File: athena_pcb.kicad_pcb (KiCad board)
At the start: 2 copper layers, 40.5 x 23.8 mm, 36 parts, among them J2 Conn_01x04, SW1 SW_Push, U1 NRF5340-QKAA-R7, U2 BME280, Y1 32MHz, Y2 32.768kHz

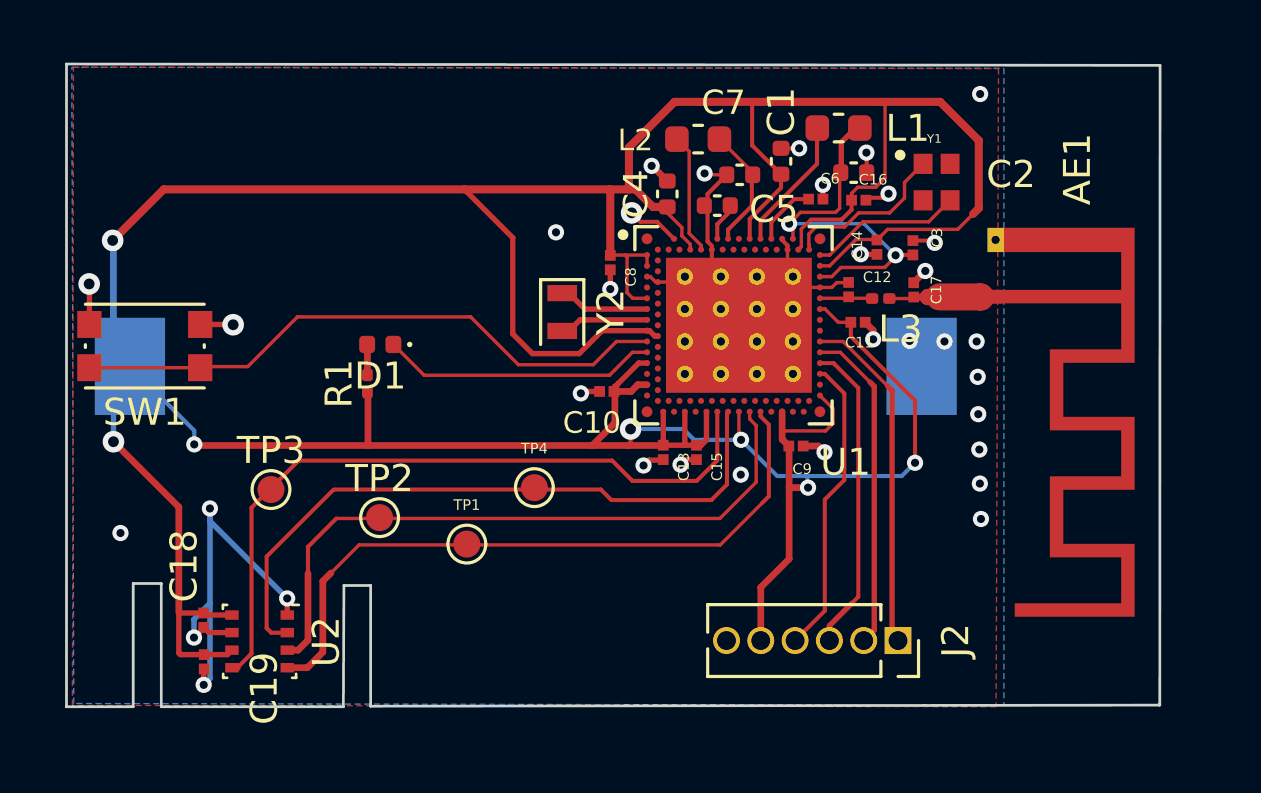
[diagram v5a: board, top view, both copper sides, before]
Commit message: Updated tracks to 6mils where possible
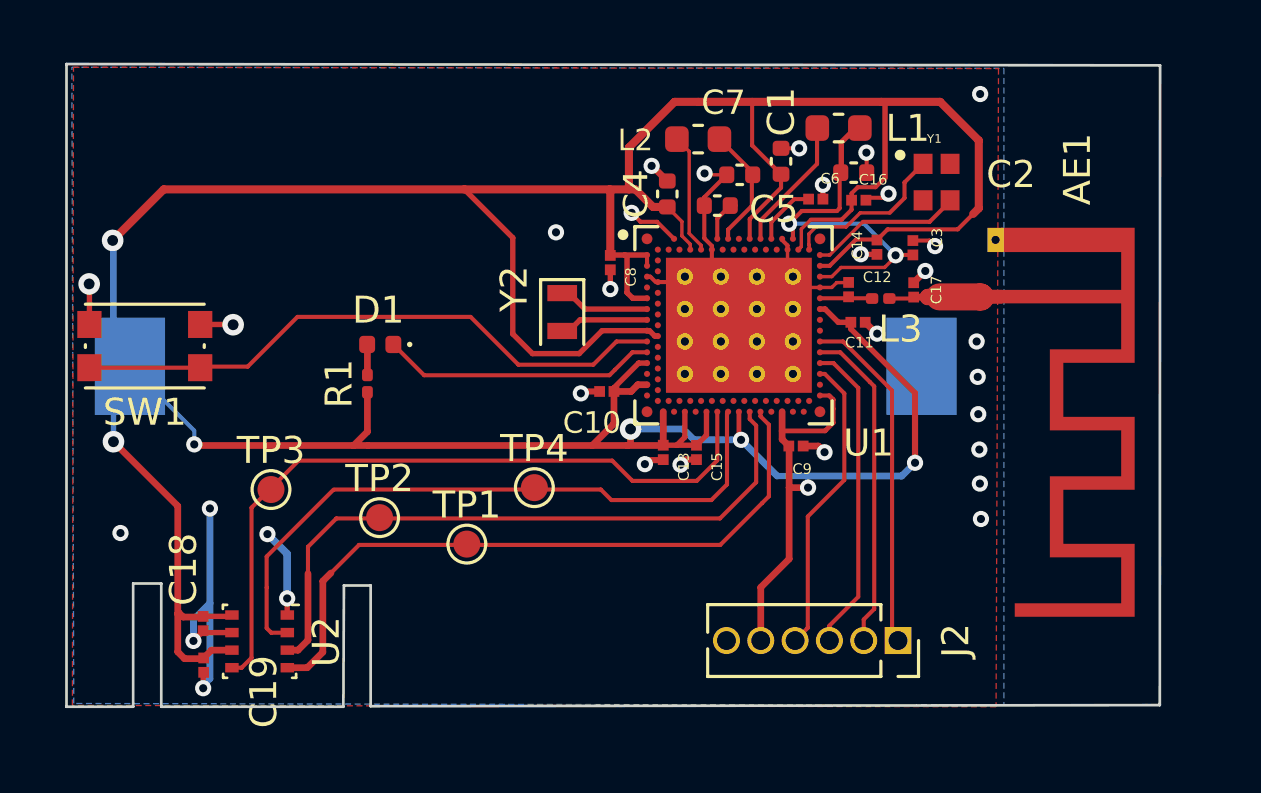
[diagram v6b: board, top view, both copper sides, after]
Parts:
- moved C19 0.13 mm to (96.5, 103.3)
- moved C18 0.13 mm to (96.5, 101.8)
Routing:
- net GND: track 51.3 -> 49.7 mm, vias 34 -> 32

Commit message: Added edge clearence, transmission line width to match with pcb antenna feed
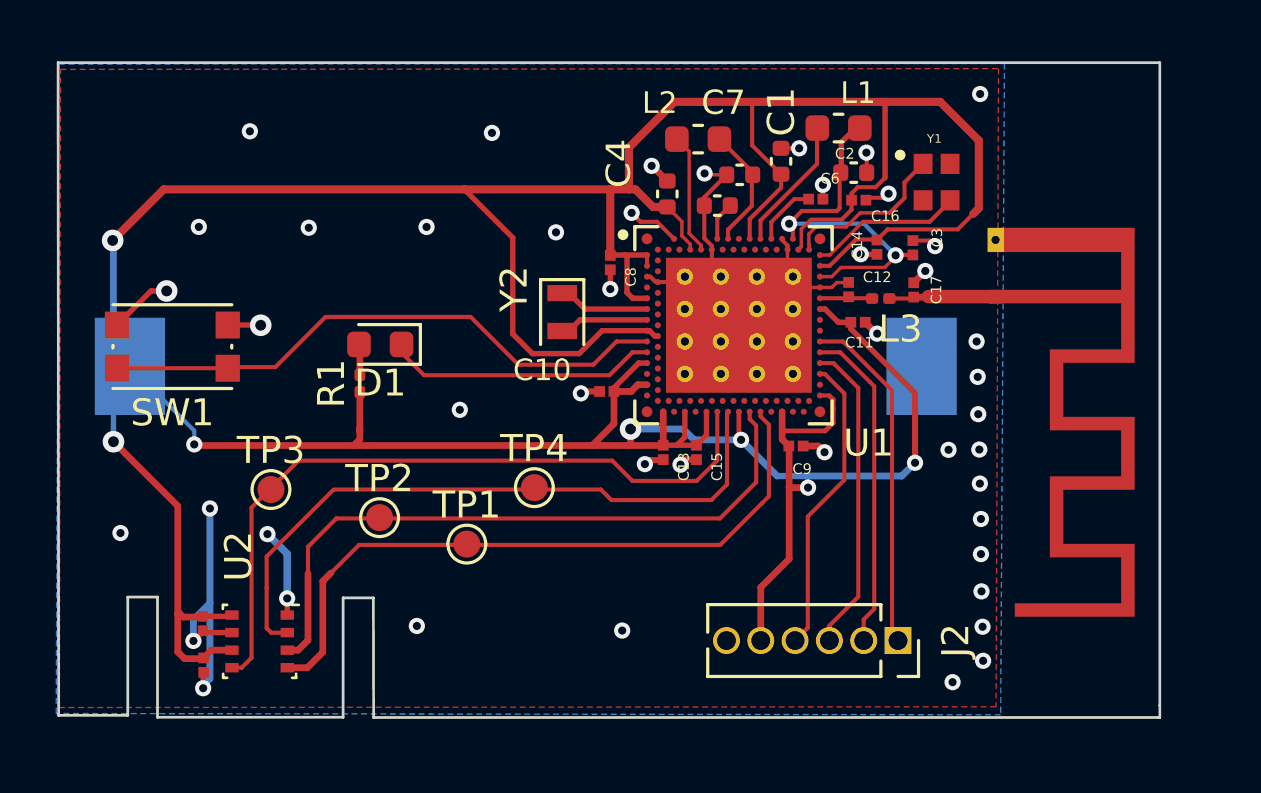
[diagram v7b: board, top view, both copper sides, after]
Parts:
- C5, C7: value 1.0uF -> 1uF
- D1: footprint LED_SMD:LED_0402_1005Metric -> LED_SMD:LED_0603_1608Metric
- moved SW1 1.02 mm to (95.4, 91.5)
- moved R1 0.28 mm to (102.3, 92.9)
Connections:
- U1 pad AK20: /P0.23 -> unconnected-(U1C-P0.23-PadAK20)
- U1 pad AL27: /P0.24 -> unconnected-(U1C-P0.24-PadAL27)
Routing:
- net GND: track 49.7 -> 51.0 mm, vias 32 -> 46
- net /P0.02: track 22.5 -> 21.5 mm
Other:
- board size 40.5 x 23.8 mm -> 40.8 x 24.2 mm

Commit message: Version sent to PCB manufacturer
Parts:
- added REF**: MountingHole_2.2mm_M2_DIN965, MountingHole:MountingHole_2.2mm_M2_DIN965, F.Cu at (94.6, 84.0)
- L1, L2: footprint Inductor_SMD:L_0603_1608Metric -> LQM18DN100M70L:INDC1608X95N
- L3: footprint Inductor_SMD:L_0201_0603Metric -> LQP03HQ2N2B02D:IND_LQP03HQ2N2B02D
- R1: value 220R -> 200R; footprint Resistor_SMD:R_0201_0603Metric -> Resistor_SMD:R_0402_1005Metric
- Y2: footprint Crystal:Crystal_SMD_2012-2Pin_2.0x1.2mm -> CM8V-T1A-32.768KHZ-9PF-20PPM-TA-QC:XTAL_CM8V-T1A-32.768KHZ-9PF-20PPM-TA-QC
- moved J2 0.60 mm to (122.2, 103.0)
- moved R1 0.53 mm to (102.3, 93.4)
- moved Y2 0.17 mm to (109.6, 90.2)
- moved Y1 0.11 mm to (123.5, 85.5)
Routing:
- net /SWDCLK: track 12.8 -> 13.4 mm
- net /RESETN: track 11.6 -> 12.2 mm
- net /SWDIO: track 12.1 -> 12.7 mm
- net /P0.28: track 11.1 -> 11.7 mm
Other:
- board text added: "YKS"
